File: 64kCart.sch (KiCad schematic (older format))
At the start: 6 parts, among them U1 27C512, U2 74LS173, U3 74LS04

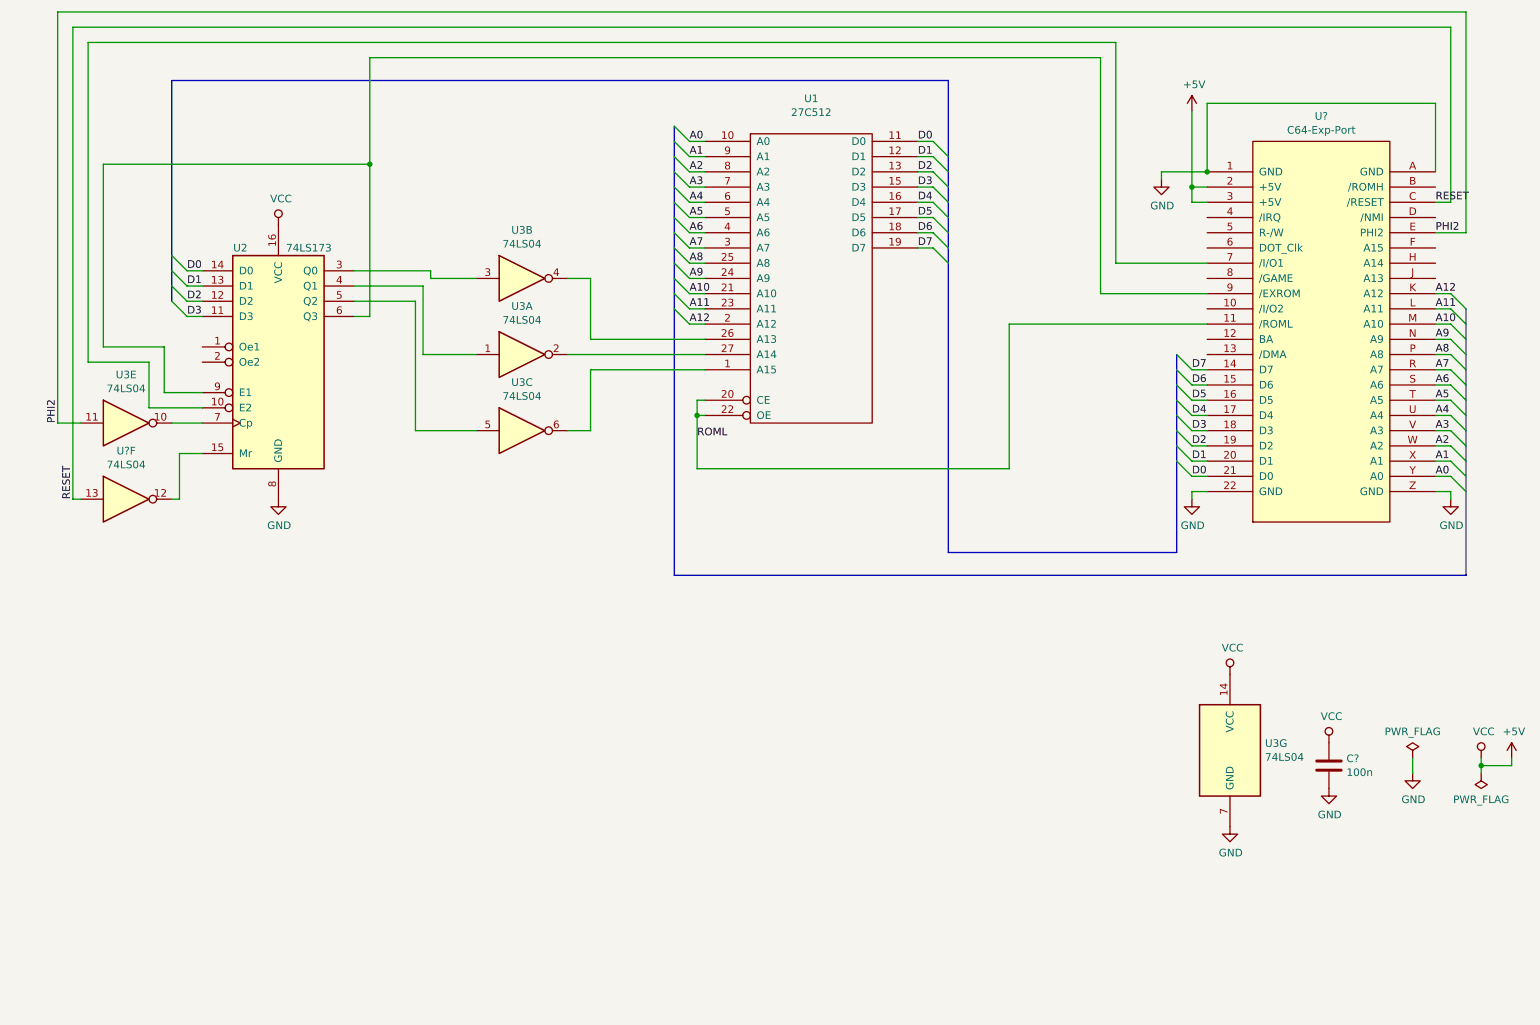
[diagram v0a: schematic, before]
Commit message: Assigned first footprints.
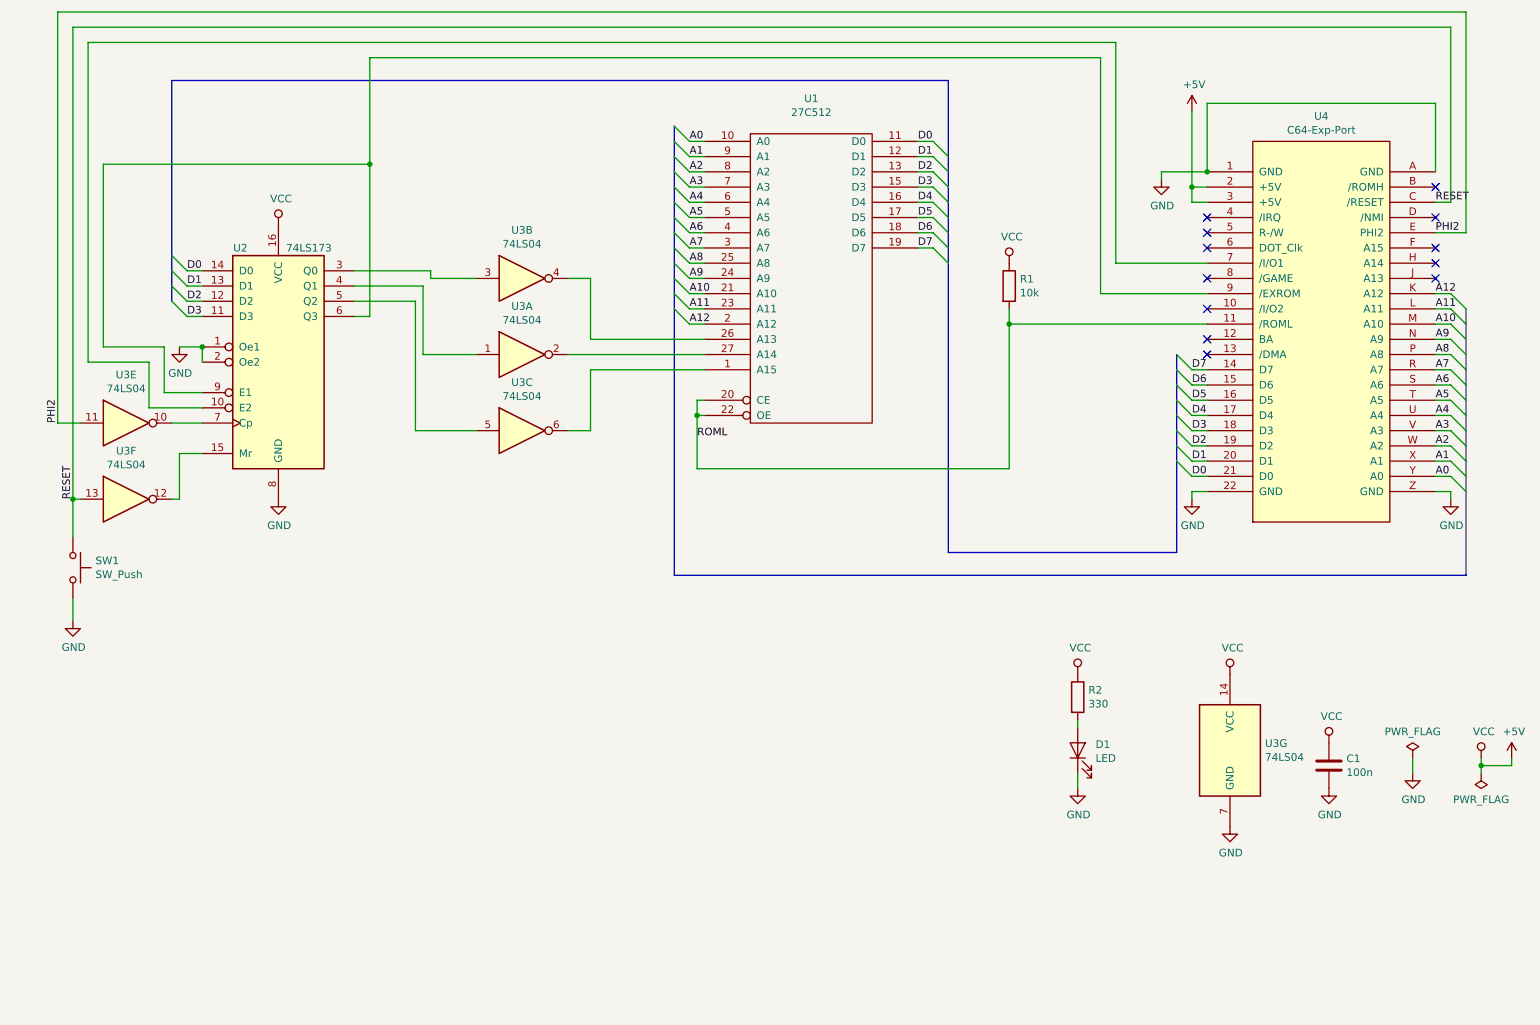
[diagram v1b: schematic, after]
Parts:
- added D1: LED, LEDs:LED_D5.0mm, symbol device:LED
- added R1: 10k, Resistors_THT:R_Axial_DIN0207_L6.3mm_D2.5mm_P7.62mm_Horizontal, symbol device:R
- added R2: 330, Resistors_THT:R_Axial_DIN0207_L6.3mm_D2.5mm_P7.62mm_Horizontal, symbol device:R
- added SW1: SW_Push, Buttons_Switches_THT:SW_Tactile_SPST_Angled_PTS645Vx83-2LFS, symbol Switch:SW_Push
- C1: renamed from C?; footprint (none) -> Capacitors_THT:C_Disc_D4.3mm_W1.9mm_P5.00mm
- U1: footprint (none) -> Housings_DIP:DIP-28_W15.24mm_Socket
- U2: footprint (none) -> Housings_DIP:DIP-16_W7.62mm_Socket
- U3: footprint (none) -> Housings_DIP:DIP-14_W7.62mm_Socket
- U3: renamed from U?; footprint (none) -> Housings_DIP:DIP-14_W7.62mm_Socket
- U4: renamed from U?; footprint MODULE -> 64kCart:C64-Cart-NoSilkS
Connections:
- net +5V: now also R1.1, R2.1
- net GND: now also U2.1 (Oe1), U2.2 (Oe2), D1.1 (K), SW1.2
- net RESET: now also SW1.1
- net ROML: now also R1.2
- new net: D1.2 (A), R2.2
- no-connect marks 0 -> 12
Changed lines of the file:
@@
 $EndDescr
 $Comp
-L 64kCart:C64-Exp-Port U?
+L 64kCart:C64-Exp-Port U4
 U 1 1 5CD17095
 P 9400 3000
-F 0 "U?" H 9400 4415 50  0000 C CNN
+F 0 "U4" H 9400 4415 50  0000 C CNN
 F 1 "C64-Exp-Port" H 9400 4324 50  0000 C CNN
-F 2 "MODULE" H 9400 1550 50  0001 C CNN
+F 2 "64kCart:C64-Cart-NoSilkS" H 9400 1550 50  0001 C CNN
 F 3 "" H 9400 1450 50  0001 C CNN
 	1    9400 3000
@@
 F 0 "U1" H 6050 3831 50  0000 C CNN
 F 1 "27C512" H 6050 3740 50  0000 C CNN
-F 2 "" H 6050 2650 50  0001 C CNN
+F 2 "Housings_DIP:DIP-28_W15.24mm_Socket" H 6050 2650 50  0001 C CNN
 F 3 "" H 6050 2650 50  0001 C CNN
 	1    6050 2650
@@
 F 0 "U3" H 4150 3467 50  0000 C CNN
 F 1 "74LS04" H 4150 3376 50  0000 C CNN
-F 2 "" H 4150 3150 50  0001 C CNN
+F 2 "Housings_DIP:DIP-14_W7.62mm_Socket" H 4150 3150 50  0001 C CNN
 F 3 "http://www.ti.com/lit/gpn/sn74LS04" H 4150 3150 50  0001 C CNN
 	1    4150 3150
@@
 $EndComp
 $Comp
-L power:PWR_FLAG #FLG?
+L power:PWR_FLAG #FLG0101
 U 1 1 5CD19A15
 P 10000 5800
-F 0 "#FLG?" H 10000 5875 50  0001 C CNN
+F 0 "#FLG0101" H 10000 5875 50  0001 C CNN
 F 1 "PWR_FLAG" H 10000 5973 50  0000 C CNN
 F 2 "" H 10000 5800 50  0001 C CNN
@@
 $EndComp
 $Comp
-L power:GND #PWR?
+L power:GND #PWR0101
 U 1 1 5CD1A439
 P 10000 5900
-F 0 "#PWR?" H 10000 5650 50  0001 C CNN
+F 0 "#PWR0101" H 10000 5650 50  0001 C CNN
 F 1 "GND" H 10005 5727 50  0000 C CNN
 F 2 "" H 10000 5900 50  0001 C CNN
@@
 $EndComp
 $Comp
-L power:PWR_FLAG #FLG?
+L power:PWR_FLAG #FLG0102
 U 1 1 5CD1A68F
 P 10450 5900
-F 0 "#FLG?" H 10450 5975 50  0001 C CNN
+F 0 "#FLG0102" H 10450 5975 50  0001 C CNN
 F 1 "PWR_FLAG" H 10450 6073 50  0000 C CNN
 F 2 "" H 10450 5900 50  0001 C CNN
@@
 $EndComp
 $Comp
-L power:VCC #PWR?
+L power:VCC #PWR0102
 U 1 1 5CD1B5F5
 P 10450 5800
-F 0 "#PWR?" H 10450 5650 50  0001 C CNN
+F 0 "#PWR0102" H 10450 5650 50  0001 C CNN
 F 1 "VCC" H 10467 5973 50  0000 C CNN
 F 2 "" H 10450 5800 50  0001 C CNN
@@
 $EndComp
 $Comp
-L power:+5V #PWR?
+L power:+5V #PWR0103
 U 1 1 5CD1BB8E
 P 10650 5800
-F 0 "#PWR?" H 10650 5650 50  0001 C CNN
+F 0 "#PWR0103" H 10650 5650 50  0001 C CNN
 F 1 "+5V" H 10665 5973 50  0000 C CNN
 F 2 "" H 10650 5800 50  0001 C CNN
@@
 	10450 5850 10450 5900
 $Comp
-L device:C C?
+L device:C C1
 U 1 1 5CD1C699
 P 9450 5850
-F 0 "C?" H 9565 5896 50  0000 L CNN
+F 0 "C1" H 9565 5896 50  0000 L CNN
 F 1 "100n" H 9565 5805 50  0000 L CNN
-F 2 "" H 9488 5700 50  0001 C CNN
+F 2 "Capacitors_THT:C_Disc_D4.3mm_W1.9mm_P5.00mm" H 9488 5700 50  0001 C CNN
 F 3 "~" H 9450 5850 50  0001 C CNN
 	1    9450 5850
@@
 $EndComp
 $Comp
-L power:GND #PWR?
+L power:GND #PWR0104
 U 1 1 5CD1C82E
 P 9450 6000
-F 0 "#PWR?" H 9450 5750 50  0001 C CNN
+F 0 "#PWR0104" H 9450 5750 50  0001 C CNN
 F 1 "GND" H 9455 5827 50  0000 C CNN
 F 2 "" H 9450 6000 50  0001 C CNN
@@
 $EndComp
 $Comp
-L power:VCC #PWR?
+L power:VCC #PWR0105
 U 1 1 5CD1CB89
 P 9450 5700
-F 0 "#PWR?" H 9450 5550 50  0001 C CNN
+F 0 "#PWR0105" H 9450 5550 50  0001 C CNN
 F 1 "VCC" H 9467 5873 50  0000 C CNN
 F 2 "" H 9450 5700 50  0001 C CNN
@@
 $EndComp
 $Comp
-L power:GND #PWR?
+L power:GND #PWR0106
 U 1 1 5CD1CEC9
 P 10250 4100
-F 0 "#PWR?" H 10250 3850 50  0001 C CNN
+F 0 "#PWR0106" H 10250 3850 50  0001 C CNN
 F 1 "GND" H 10255 3927 50  0000 C CNN
 F 2 "" H 10250 4100 50  0001 C CNN
@@
 $EndComp
 $Comp
-L power:GND #PWR?
+L power:GND #PWR0107
 U 1 1 5CD1D621
 P 8550 4100
-F 0 "#PWR?" H 8550 3850 50  0001 C CNN
+F 0 "#PWR0107" H 8550 3850 50  0001 C CNN
 F 1 "GND" H 8555 3927 50  0000 C CNN
 F 2 "" H 8550 4100 50  0001 C CNN
@@
 Connection ~ 8650 1950
 $Comp
-L power:GND #PWR?
+L power:GND #PWR0108
 U 1 1 5CD1F7D9
 P 8350 2000
-F 0 "#PWR?" H 8350 1750 50  0001 C CNN
+F 0 "#PWR0108" H 8350 1750 50  0001 C CNN
 F 1 "GND" H 8355 1827 50  0000 C CNN
 F 2 "" H 8350 2000 50  0001 C CNN
@@
 $EndComp
 $Comp
-L power:+5V #PWR?
+L power:+5V #PWR0109
 U 1 1 5CD1FB09
 P 8550 1550
-F 0 "#PWR?" H 8550 1400 50  0001 C CNN
+F 0 "#PWR0109" H 8550 1400 50  0001 C CNN
 F 1 "+5V" H 8565 1723 50  0000 C CNN
 F 2 "" H 8550 1550 50  0001 C CNN
@@
 $EndComp
 $Comp
-L power:GND #PWR?
+L power:GND #PWR0110
 U 1 1 5CD1FE90
 P 2550 4100
-F 0 "#PWR?" H 2550 3850 50  0001 C CNN
+F 0 "#PWR0110" H 2550 3850 50  0001 C CNN
 F 1 "GND" H 2555 3927 50  0000 C CNN
 F 2 "" H 2550 4100 50  0001 C CNN
@@
 $EndComp
 $Comp
-L power:VCC #PWR?
+L power:VCC #PWR0111
 U 1 1 5CD202F2
 P 2550 2300
-F 0 "#PWR?" H 2550 2150 50  0001 C CNN
+F 0 "#PWR0111" H 2550 2150 50  0001 C CNN
 F 1 "VCC" H 2567 2473 50  0000 C CNN
 F 2 "" H 2550 2300 50  0001 C CNN
@@
 F 0 "U3" H 9030 5796 50  0000 L CNN
 F 1 "74LS04" H 9030 5705 50  0000 L CNN
-F 2 "" H 8800 5750 50  0001 C CNN
+F 2 "Housings_DIP:DIP-14_W7.62mm_Socket" H 8800 5750 50  0001 C CNN
 F 3 "http://www.ti.com/lit/gpn/sn74LS04" H 8800 5750 50  0001 C CNN
 	7    8800 5750
@@
 $EndComp
 $Comp
-L power:GND #PWR?
+L power:GND #PWR0112
 U 1 1 5CD2295D
 P 8800 6250
-F 0 "#PWR?" H 8800 6000 50  0001 C CNN
+F 0 "#PWR0112" H 8800 6000 50  0001 C CNN
 F 1 "GND" H 8805 6077 50  0000 C CNN
 F 2 "" H 8800 6250 50  0001 C CNN
@@
 $EndComp
 $Comp
-L power:VCC #PWR?
+L power:VCC #PWR0113
 U 1 1 5CD23406
 P 8800 5250
-F 0 "#PWR?" H 8800 5100 50  0001 C CNN
+F 0 "#PWR0113" H 8800 5100 50  0001 C CNN
 F 1 "VCC" H 8817 5423 50  0000 C CNN
 F 2 "" H 8800 5250 50  0001 C CNN
@@
 F 0 "U3" H 4150 2967 50  0000 C CNN
 F 1 "74LS04" H 4150 2876 50  0000 C CNN
-F 2 "" H 4150 2650 50  0001 C CNN
+F 2 "Housings_DIP:DIP-14_W7.62mm_Socket" H 4150 2650 50  0001 C CNN
 F 3 "http://www.ti.com/lit/gpn/sn74LS04" H 4150 2650 50  0001 C CNN
 	2    4150 2650
@@
 F 0 "U3" H 4150 3967 50  0000 C CNN
 F 1 "74LS04" H 4150 3876 50  0000 C CNN
-F 2 "" H 4150 3650 50  0001 C CNN
+F 2 "Housings_DIP:DIP-14_W7.62mm_Socket" H 4150 3650 50  0001 C CNN
 F 3 "http://www.ti.com/lit/gpn/sn74LS04" H 4150 3650 50  0001 C CNN
 	3    4150 3650
@@
 F 0 "U2" H 2300 3950 50  0000 C CNN
 F 1 "74LS173" H 2750 3950 50  0000 C CNN
-F 2 "" H 2550 3200 50  0001 C CNN
+F 2 "Housings_DIP:DIP-16_W7.62mm_Socket" H 2550 3200 50  0001 C CNN
 F 3 "http://www.ti.com/lit/gpn/sn74LS173" H 2550 3200 50  0001 C CNN
 	1    2550 3200
@@
 F 0 "U3" H 1550 3917 50  0000 C CNN
 F 1 "74LS04" H 1550 3826 50  0000 C CNN
-F 2 "" H 1550 3600 50  0001 C CNN
+F 2 "Housings_DIP:DIP-14_W7.62mm_Socket" H 1550 3600 50  0001 C CNN
 F 3 "http://www.ti.com/lit/gpn/sn74LS04" H 1550 3600 50  0001 C CNN
 	5    1550 3600
@@
 	1100 3600 1250 3600
 $Comp
-L Logic_74xx:74LS04 U?
+L Logic_74xx:74LS04 U3
 U 6 1 5CDB2A53
 P 1550 4100
-F 0 "U?" H 1550 4417 50  0000 C CNN
+F 0 "U3" H 1550 4417 50  0000 C CNN
 F 1 "74LS04" H 1550 4326 50  0000 C CNN
-F 2 "" H 1550 4100 50  0001 C CNN
+F 2 "Housings_DIP:DIP-14_W7.62mm_Socket" H 1550 4100 50  0001 C CNN
 F 3 "http://www.ti.com/lit/gpn/sn74LS04" H 1550 4100 50  0001 C CNN
 	6    1550 4100
@@
 Wire Bus Line
 	5150 4600 10350 4600
+$Comp
+L power:GND #PWR0114
+U 1 1 5CE0DC44
+P 1900 3100
+F 0 "#PWR0114" H 1900 2850 50  0001 C CNN
+F 1 "GND" H 1905 2927 50  0000 C CNN
+F 2 "" H 1900 3100 50  0001 C CNN
+F 3 "" H 1900 3100 50  0001 C CNN
+	1    1900 3100
+	1    0    0    -1
+$EndComp
+Wire Wire Line
+	1900 3100 2050 3100
+Wire Wire Line
+	2050 3100 2050 3200
+Connection ~ 2050 3100
+NoConn ~ 8650 2250
+NoConn ~ 8650 2350
+NoConn ~ 8650 2450
+NoConn ~ 8650 2650
+NoConn ~ 8650 2850
+NoConn ~ 8650 3150
+NoConn ~ 8650 3050
+NoConn ~ 10150 2050
+NoConn ~ 10150 2250
+NoConn ~ 10150 2450
+NoConn ~ 10150 2550
+NoConn ~ 10150 2650
+$Comp
+L device:R R1
+U 1 1 5CE641BB
+P 7350 2700
+F 0 "R1" H 7420 2746 50  0000 L CNN
+F 1 "10k" H 7420 2655 50  0000 L CNN
+F 2 "Resistors_THT:R_Axial_DIN0207_L6.3mm_D2.5mm_P7.62mm_Horizontal" V 7280 2700 50  0001 C CNN
+F 3 "~" H 7350 2700 50  0001 C CNN
+	1    7350 2700
+	1    0    0    -1
+$EndComp
+Wire Wire Line
+	7350 2850 7350 2950
+Connection ~ 7350 2950
+$Comp
+L power:VCC #PWR0115
+U 1 1 5CE6AB9F
+P 7350 2550
+F 0 "#PWR0115" H 7350 2400 50  0001 C CNN
+F 1 "VCC" H 7367 2723 50  0000 C CNN
+F 2 "" H 7350 2550 50  0001 C CNN
+F 3 "" H 7350 2550 50  0001 C CNN
+	1    7350 2550
+	1    0    0    -1
+$EndComp
+$Comp
+L device:R R2
+U 1 1 5CE6B617
+P 7800 5400
+F 0 "R2" H 7870 5446 50  0000 L CNN
+F 1 "330" H 7870 5355 50  0000 L CNN
+F 2 "Resistors_THT:R_Axial_DIN0207_L6.3mm_D2.5mm_P7.62mm_Horizontal" V 7730 5400 50  0001 C CNN
+F 3 "~" H 7800 5400 50  0001 C CNN
+	1    7800 5400
+	1    0    0    -1
+$EndComp
+$Comp
+L power:VCC #PWR0116
+U 1 1 5CE6BAE1
+P 7800 5250
+F 0 "#PWR0116" H 7800 5100 50  0001 C CNN
+F 1 "VCC" H 7817 5423 50  0000 C CNN
+F 2 "" H 7800 5250 50  0001 C CNN
+F 3 "" H 7800 5250 50  0001 C CNN
+	1    7800 5250
+	1    0    0    -1
+$EndComp
+$Comp
+L device:LED D1
+U 1 1 5CE72C00
+P 7800 5750
+F 0 "D1" V 7839 5633 50  0000 R CNN
+F 1 "LED" V 7748 5633 50  0000 R CNN
+F 2 "LEDs:LED_D5.0mm" H 7800 5750 50  0001 C CNN
+F 3 "~" H 7800 5750 50  0001 C CNN
+	1    7800 5750
+	0    -1   -1   0
+$EndComp
+$Comp
+L power:GND #PWR0117
+U 1 1 5CE7311F
+P 7800 6000
+F 0 "#PWR0117" H 7800 5750 50  0001 C CNN
+F 1 "GND" H 7805 5827 50  0000 C CNN
+F 2 "" H 7800 6000 50  0001 C CNN
+F 3 "" H 7800 6000 50  0001 C CNN
+	1    7800 6000
+	1    0    0    -1
+$EndComp
+Wire Wire Line
+	7800 5600 7800 5550
+Wire Wire Line
+	7800 6000 7800 5900
+$Comp
+L Switch:SW_Push SW1
+U 1 1 5CE92746
+P 1200 4550
+F 0 "SW1" V 1154 4698 50  0000 L CNN
+F 1 "SW_Push" V 1245 4698 50  0000 L CNN
+F 2 "Buttons_Switches_THT:SW_Tactile_SPST_Angled_PTS645Vx83-2LFS" H 1200 4750 50  0001 C CNN
+F 3 "~" H 1200 4750 50  0001 C CNN
+	1    1200 4550
+	0    1    1    0
+$EndComp
+$Comp
+L power:GND #PWR0118
+U 1 1 5CE94349
+P 1200 4900
+F 0 "#PWR0118" H 1200 4650 50  0001 C CNN
+F 1 "GND" H 1205 4727 50  0000 C CNN
+F 2 "" H 1200 4900 50  0001 C CNN
+F 3 "" H 1200 4900 50  0001 C CNN
+	1    1200 4900
+	1    0    0    -1
+$EndComp
+Wire Wire Line
+	1200 4100 1200 4350
+Connection ~ 1200 4100
+Wire Wire Line
+	1200 4750 1200 4900
 Wire Bus Line
 	1850 1350 1850 2800

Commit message: Minor improvements.
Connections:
- net IO1: now reaches U2.10 (E2), U4.7 (/I/O1)
- net EXROM: now reaches U2.6 (Q3), U2.9 (E1), U4.9 (/EXROM)
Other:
- moved on the sheet: U3B, U3C
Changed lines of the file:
@@
 EESchema Schematic File Version 4
+LIBS:64kCart-cache
 EELAYER 29 0
 EELAYER END
@@
 L Logic_74xx:74LS04 U3
 U 2 1 5CD58869
-P 4150 2650
-F 0 "U3" H 4150 2967 50  0000 C CNN
-F 1 "74LS04" H 4150 2876 50  0000 C CNN
-F 2 "Housings_DIP:DIP-14_W7.62mm_Socket" H 4150 2650 50  0001 C CNN
-F 3 "http://www.ti.com/lit/gpn/sn74LS04" H 4150 2650 50  0001 C CNN
-	2    4150 2650
+P 4150 2600
+F 0 "U3" H 4150 2917 50  0000 C CNN
+F 1 "74LS04" H 4150 2826 50  0000 C CNN
+F 2 "Housings_DIP:DIP-14_W7.62mm_Socket" H 4150 2600 50  0001 C CNN
+F 3 "http://www.ti.com/lit/gpn/sn74LS04" H 4150 2600 50  0001 C CNN
+	2    4150 2600
 	1    0    0    -1
 $EndComp
@@
 L Logic_74xx:74LS04 U3
 U 3 1 5CD62C68
-P 4150 3650
-F 0 "U3" H 4150 3967 50  0000 C CNN
-F 1 "74LS04" H 4150 3876 50  0000 C CNN
-F 2 "Housings_DIP:DIP-14_W7.62mm_Socket" H 4150 3650 50  0001 C CNN
-F 3 "http://www.ti.com/lit/gpn/sn74LS04" H 4150 3650 50  0001 C CNN
-	3    4150 3650
-	1    0    0    -1
-$EndComp
-Wire Wire Line
-	4450 2650 4600 2650
-Wire Wire Line
-	4600 2650 4600 3050
+P 4150 3700
+F 0 "U3" H 4150 4017 50  0000 C CNN
+F 1 "74LS04" H 4150 3926 50  0000 C CNN
+F 2 "Housings_DIP:DIP-14_W7.62mm_Socket" H 4150 3700 50  0001 C CNN
+F 3 "http://www.ti.com/lit/gpn/sn74LS04" H 4150 3700 50  0001 C CNN
+	3    4150 3700
+	1    0    0    -1
+$EndComp
 Wire Wire Line
 	4600 3050 5350 3050
@@
 	5350 3150 4450 3150
 Wire Wire Line
-	4600 3650 4600 3250
-Wire Wire Line
 	4600 3250 5350 3250
-Wire Wire Line
-	4450 3650 4600 3650
 $Comp
 L Logic_74xx:74LS173 U2
@@
 	3050 2700 3500 2700
 Wire Wire Line
-	3050 2600 3550 2600
-Wire Wire Line
-	3550 2600 3550 2650
-Wire Wire Line
-	3550 2650 3850 2650
-Wire Wire Line
 	3050 2800 3450 2800
-Wire Wire Line
-	3450 2800 3450 3650
-Wire Wire Line
-	3450 3650 3850 3650
 $Comp
 L Logic_74xx:74LS04 U3
@@
 Wire Wire Line
 	1200 4750 1200 4900
+Text Label 8650 2750 2    50   ~ 0
+EXROM
+Text Label 8650 2550 2    50   ~ 0
+IO1
+Text Label 8650 2950 2    50   ~ 0
+ROML
+Text Label 1800 3100 2    50   ~ 0
+EXROM
+Text Label 1700 3200 2    50   ~ 0
+IO1
+Wire Wire Line
+	3450 3700 3850 3700
+Wire Wire Line
+	3450 2800 3450 3700
+Wire Wire Line
+	4450 3700 4600 3700
+Wire Wire Line
+	4600 3250 4600 3700
+Wire Wire Line
+	3050 2600 3850 2600
+Wire Wire Line
+	4450 2600 4600 2600
+Wire Wire Line
+	4600 2600 4600 3050
 Wire Bus Line
 	1850 1350 1850 2800
